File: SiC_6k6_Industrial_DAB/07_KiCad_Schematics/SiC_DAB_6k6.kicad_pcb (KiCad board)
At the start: 6 copper layers, 340 x 250 mm, 261 parts, among them J1 HV+, J10 BoosterPack J1/J3, J11 BoosterPack J2/J4, J12 BoosterPack PWM, J13 +24V IN, J14 CAN, J15 UART, J16 RELAY/FAN, J17 INTERLOCK IN, J18 NTC1, J19 NTC2, J2 HV-, J20 PE, J21 PE_HV, J22 PE_LV, J3 SW_A, J4 SW_B, J5 LV+, J6 LV-, J7 SW_C, J8 SW_D, J9 L1 (via CT), Q1 C3M0032120K, Q2 C3M0032120K, Q3 C3M0032120K, Q4 C3M0032120K, Q5 C3M0016120K, Q6 C3M0016120K, Q7 C3M0016120K, Q8 C3M0016120K, U1 UCC21520DW, U10 LM393, U11 LM393, U12 74HC32, U13 TSR 3-24120, U14 TSR 1-2450, U15 AMS1117-3.3, U16 TCAN332, U17 ULN2003A, U18 PC817, U19 PC817, U2 UCC21520DW, U3 UCC21520DW, U4 UCC21520DW, U5 AMC1301, U6 AMC1301, U7 AMC1301, U8 TLV9062, U9 TLV9062

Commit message: DAB board: intermediate generated board file (run 23 in progress)
Co-Authored-By: Claude Fable 5.1 <noreply@anthropic.com>
Claude-Session: https://claude.ai/code/session_01TJ4PYx4qhHYB2ApeFHUZoW
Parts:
- moved J16 2.50 mm to (196.0, 176.5)

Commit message: DAB: no stub fan-out on J16, fuse holder 1 mm further from the J1 stud; run 23 board (8 errors: +24V unrouted, 1 courtyard)
Co-Authored-By: Claude Fable 5.1 <noreply@anthropic.com>
Claude-Session: https://claude.ai/code/session_01TJ4PYx4qhHYB2ApeFHUZoW
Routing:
- net +5V: track 0.00 -> 748.2 mm, vias 0 -> 20
- net GND: track 0.00 -> 518.1 mm, vias 0 -> 75
- net PROT_DIS: track 0.00 -> 431.4 mm, vias 0 -> 21
- net +12V: track 0.00 -> 375.8 mm, vias 0 -> 11
- net +3V3: track 0.00 -> 258.3 mm, vias 0 -> 2
- net VEE_Q8: track 0.00 -> 216.2 mm, vias 0 -> 4
- net V1_SE: track 0.00 -> 209.6 mm, vias 0 -> 6
- net KS_Q8: track 0.00 -> 193.8 mm, vias 0 -> 1
- net PWM1B: track 0.00 -> 192.2 mm, vias 0 -> 2
- net DSP_DIS: track 0.00 -> 191.6 mm, vias 0 -> 4
- net PWM1A: track 0.00 -> 189.4 mm, vias 0 -> 2
- net PE_HV: track 0.00 -> 188.2 mm
- net VDD_Q1: track 0.00 -> 186.2 mm, vias 0 -> 7
- net PWM3A: track 0.00 -> 177.2 mm, vias 0 -> 1
- net VDD_Q8: track 0.00 -> 176.2 mm, vias 0 -> 3
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
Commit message: DAB board: intermediate generated board file (run 24 in progress)
Co-Authored-By: Claude Fable 5.1 <noreply@anthropic.com>
Claude-Session: https://claude.ai/code/session_01TJ4PYx4qhHYB2ApeFHUZoW
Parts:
- moved F1 1.50 mm to (54.5, 70.0)
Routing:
- net +5V: track 748.2 -> 0.00 mm, vias 20 -> 0
- net GND: track 518.1 -> 0.00 mm, vias 75 -> 0
- net PROT_DIS: track 431.4 -> 0.00 mm, vias 21 -> 0
- net +12V: track 375.8 -> 0.00 mm, vias 11 -> 0
- net +3V3: track 258.3 -> 0.00 mm, vias 2 -> 0
- net VEE_Q8: track 216.2 -> 0.00 mm, vias 4 -> 0
- net V1_SE: track 209.6 -> 0.00 mm, vias 6 -> 0
- net KS_Q8: track 193.8 -> 0.00 mm, vias 1 -> 0
- net PWM1B: track 192.2 -> 0.00 mm, vias 2 -> 0
- net DSP_DIS: track 191.6 -> 0.00 mm, vias 4 -> 0
- net PWM1A: track 189.4 -> 0.00 mm, vias 2 -> 0
- net PE_HV: track 188.2 -> 0.00 mm
- net VDD_Q1: track 186.2 -> 0.00 mm, vias 7 -> 0
- net PWM3A: track 177.2 -> 0.00 mm, vias 1 -> 0
- net VDD_Q8: track 176.2 -> 0.00 mm, vias 3 -> 0
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
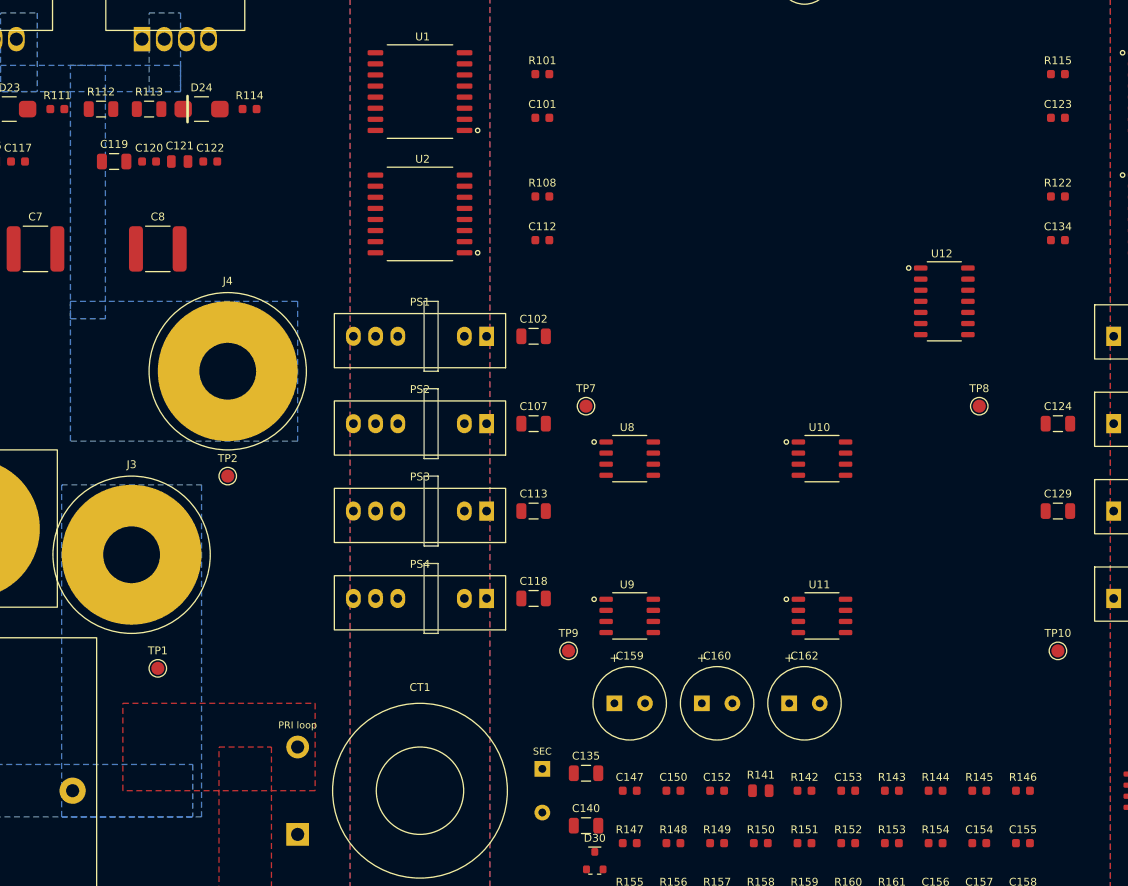
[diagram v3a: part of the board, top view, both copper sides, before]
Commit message: DAB board: run 24 result (+5V unrouted at the U4 exit channel); widen the driver-side exit channels, move J3 clear of F1, solid GND pads for C160/J16; research gap analysis and literature database
Co-Authored-By: Claude Fable 5.1 <noreply@anthropic.com>
Claude-Session: https://claude.ai/code/session_01TJ4PYx4qhHYB2ApeFHUZoW
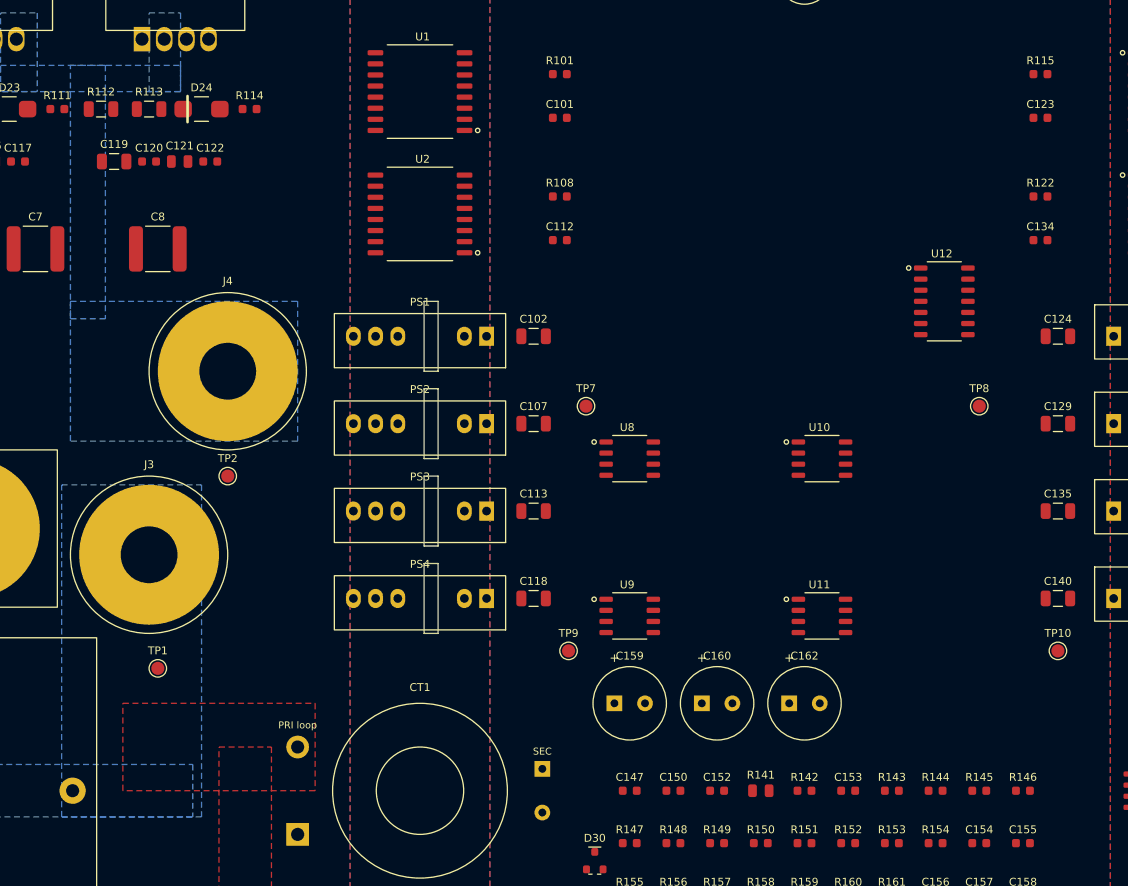
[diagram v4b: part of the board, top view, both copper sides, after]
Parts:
- moved C135 61.8 mm to (199.0, 68.0)
- moved C140 59.9 mm to (199.0, 78.0)
- moved C124 10.0 mm to (199.0, 48.0)
- moved C129 10.0 mm to (199.0, 58.0)
- moved C101 2.00 mm to (142.0, 23.0)
- moved C112 2.00 mm to (142.0, 37.0)
- moved C123 2.00 mm to (197.0, 23.0)
- moved C134 2.00 mm to (197.0, 37.0)
- moved J3 2.00 mm to (95.0, 73.0)
- moved R101 2.00 mm to (142.0, 18.0)
- moved R108 2.00 mm to (142.0, 32.0)
- moved R115 2.00 mm to (197.0, 18.0)
- moved R122 2.00 mm to (197.0, 32.0)

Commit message: WIP snapshot: research modules in progress (agents writing), DAB board run 26 result files and run-27 intermediate board
Co-Authored-By: Claude Fable 5.1 <noreply@anthropic.com>
Claude-Session: https://claude.ai/code/session_01TJ4PYx4qhHYB2ApeFHUZoW
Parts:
- moved U10 8.00 mm to (180.0, 62.0)
- moved U11 8.00 mm to (180.0, 80.0)
- moved TP2 6.00 mm to (110.0, 64.0)

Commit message: DAB 6-layer board: routing run 27 - DRC 0 errors, 0 unconnected items (63 silkscreen/dangling warnings)
Co-Authored-By: Claude Fable 5.1 <noreply@anthropic.com>
Claude-Session: https://claude.ai/code/session_01TJ4PYx4qhHYB2ApeFHUZoW
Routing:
- net +5V: track 0.00 -> 761.4 mm, vias 0 -> 24
- net GND: track 0.00 -> 511.4 mm, vias 0 -> 80
- net PROT_DIS: track 0.00 -> 440.4 mm, vias 0 -> 16
- net +12V: track 0.00 -> 364.8 mm, vias 0 -> 9
- net +24V: track 0.00 -> 265.8 mm, vias 0 -> 6
- net +3V3: track 0.00 -> 259.8 mm, vias 0 -> 2
- net V1_SE: track 0.00 -> 229.1 mm, vias 0 -> 7
- net VEE_Q3: track 0.00 -> 219.4 mm, vias 0 -> 6
- net VEE_Q8: track 0.00 -> 216.2 mm, vias 0 -> 4
- net KS_Q1: track 0.00 -> 195.8 mm, vias 0 -> 2
- net KS_Q8: track 0.00 -> 193.8 mm, vias 0 -> 1
- net PWM1B: track 0.00 -> 192.7 mm, vias 0 -> 2
- net DSP_DIS: track 0.00 -> 191.1 mm, vias 0 -> 2
- net PE_HV: track 0.00 -> 188.2 mm
- net VDD_Q1: track 0.00 -> 181.7 mm, vias 0 -> 6
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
